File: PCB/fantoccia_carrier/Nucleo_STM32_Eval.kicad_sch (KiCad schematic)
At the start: 11 parts, among them J1 BU2450SM-JJ-GTR, U1 NUCLEO144-H743ZI

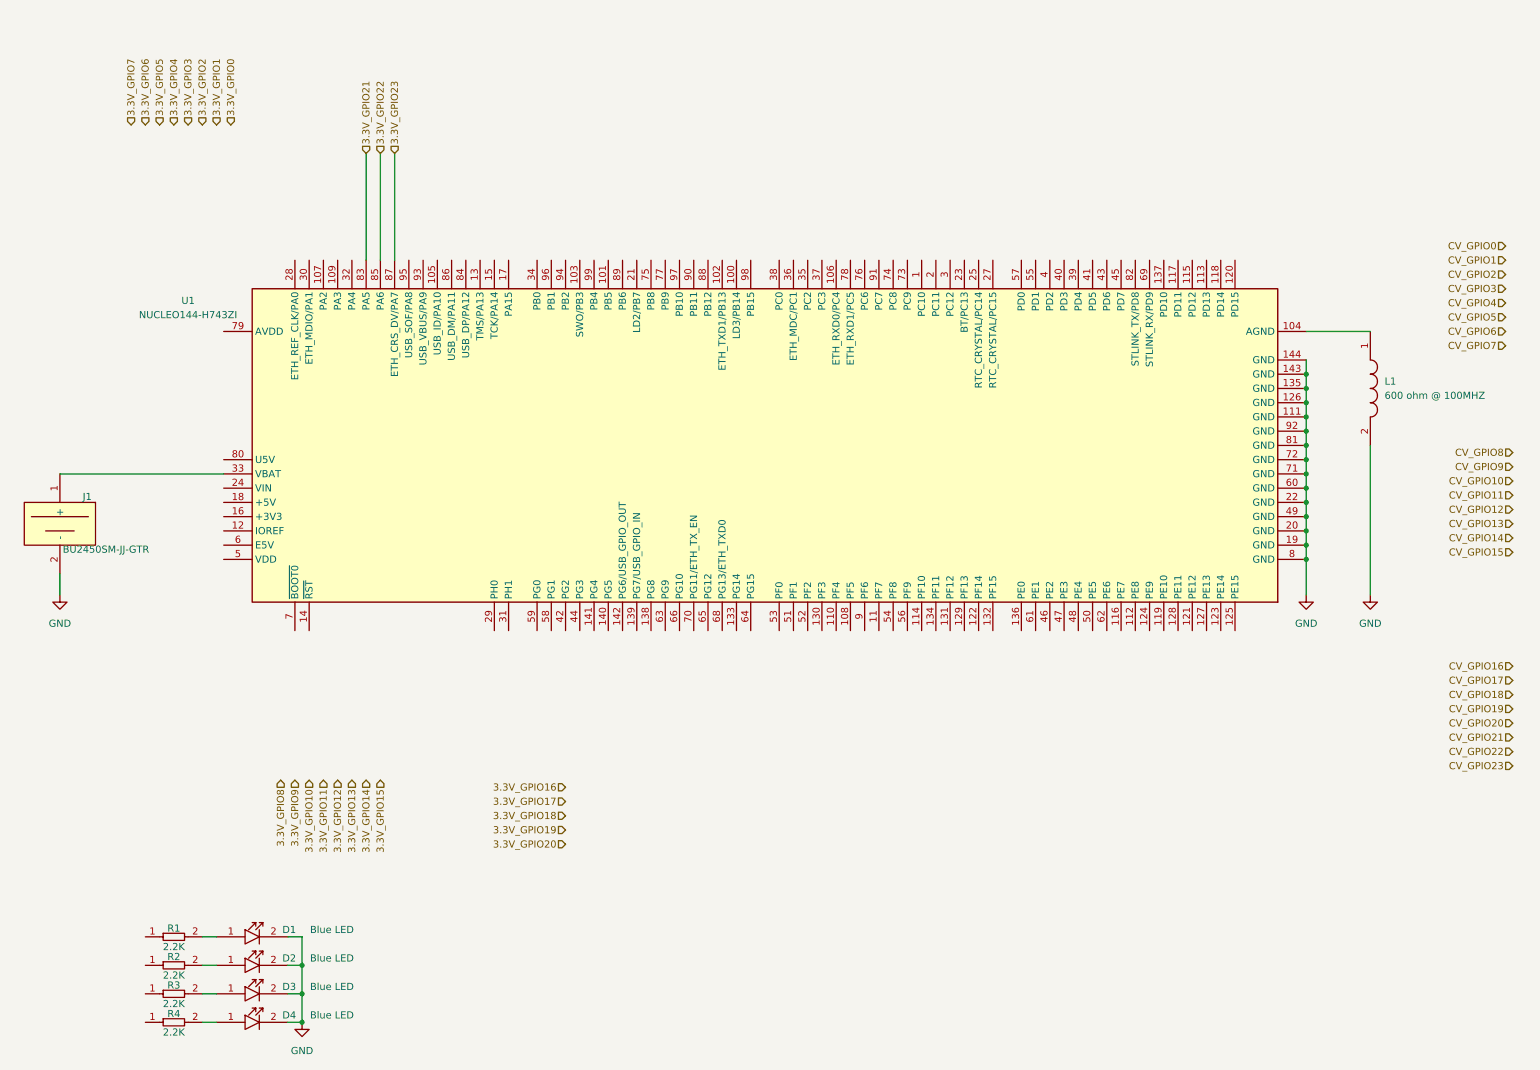
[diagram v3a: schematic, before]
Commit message: PCB and Pinout
Progress made with PCB wiring eval board pins to pheonix connectors. Pinout almost completely chosen but subject to revision !
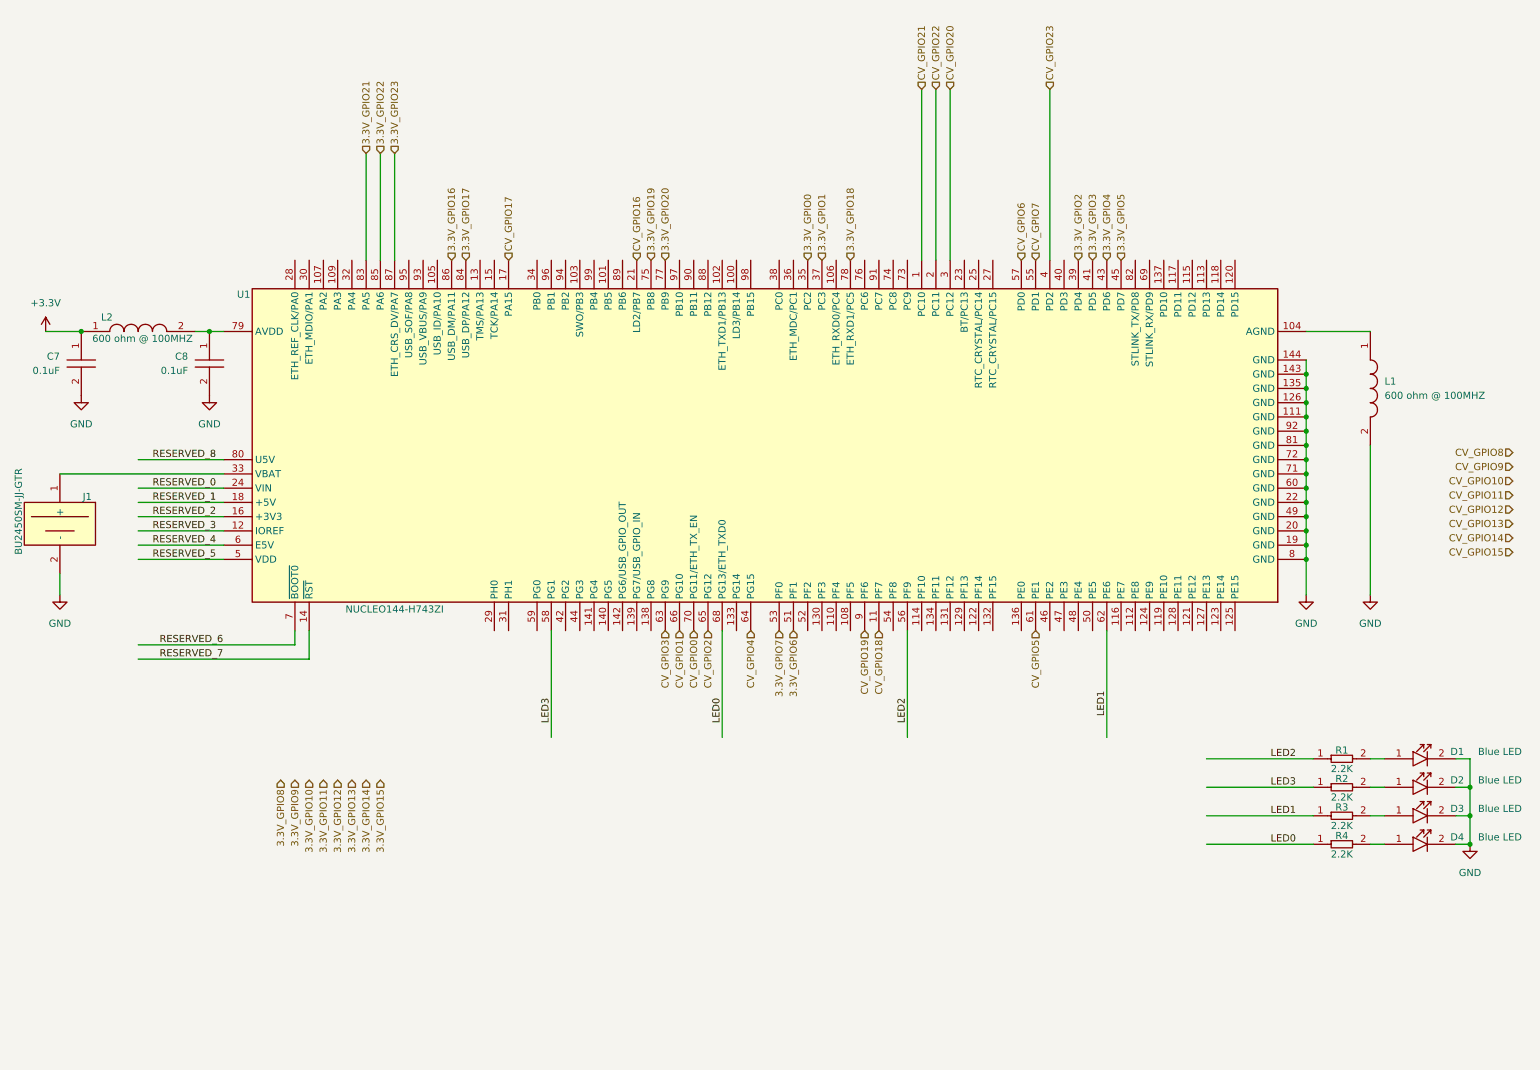
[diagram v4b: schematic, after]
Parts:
- added C7, C8: CGA3E2X7R1H104K080AA, AVR-KiCAD-Lib-Capacitors:C0603, symbol AVR-KiCAD-Lib-Capacitors:CGA3E2X7R1H104K080AA
- added L2: HZ0805E601R-10, AVR-KiCAD-Lib-Inductors:HZ0805E601R-10, symbol AVR-KiCAD-Lib-Inductors:HZ0805E601R-10
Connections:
- net 3.3V_GPIO0: now also U1.35 (PC2)
- net 3.3V_GPIO1: now also U1.37 (PC3)
- net 3.3V_GPIO16: now also U1.86 (USB_DM/PA11)
- net 3.3V_GPIO17: now also U1.84 (USB_DP/PA12)
- net 3.3V_GPIO18: now also U1.78 (ETH_RXD1/PC5)
- net 3.3V_GPIO19: now also U1.75 (PB8)
- net 3.3V_GPIO2: now also U1.39 (PD4)
- net 3.3V_GPIO20: now also U1.77 (PB9)
- net 3.3V_GPIO3: now also U1.41 (PD5)
- net 3.3V_GPIO4: now also U1.43 (PD6)
- net 3.3V_GPIO5: now also U1.45 (PD7)
- net 3.3V_GPIO6: now also U1.51 (PF1)
- net 3.3V_GPIO7: now also U1.53 (PF0)
- net CV_GPIO0: now also U1.70 (PG11/ETH_TX_EN)
- net CV_GPIO1: now also U1.66 (PG10)
- net CV_GPIO16: now also U1.21 (LD2/PB7)
- net CV_GPIO17: now also U1.17 (PA15)
- net CV_GPIO18: now also U1.11 (PF7)
- net CV_GPIO19: now also U1.9 (PF6)
- net CV_GPIO2: now also U1.65 (PG12)
- net CV_GPIO20: now also U1.3 (PC12)
- net CV_GPIO21: now also U1.1 (PC10)
- net CV_GPIO22: now also U1.2 (PC11)
- net CV_GPIO23: now also U1.4 (PD2)
- net CV_GPIO3: now also U1.63 (PG9)
- net CV_GPIO4: now also U1.64 (PG15)
- net CV_GPIO5: now also U1.61 (PE1)
- net CV_GPIO6: now also U1.57 (PD0)
- net CV_GPIO7: now also U1.55 (PD1)
- net GND: now also C7.2, C8.2
- net LED0: now reaches R4.1
- net LED0: now also U1.68 (PG13/ETH_TXD0)
- net RESERVED_3: now reaches U1.12 (IOREF)
- net RESERVED_7: now reaches U1.14 (~{RST})
- net RESERVED_2: now reaches U1.16 (+3V3)
- net RESERVED_1: now reaches U1.18 (+5V)
- net RESERVED_0: now reaches U1.24 (VIN)
- net RESERVED_5: now reaches U1.5 (VDD)
- net LED2: now reaches U1.56 (PF9)
- net LED2: now also R1.1
- net LED3: now reaches U1.58 (PG1)
- net LED3: now also R2.1
- net RESERVED_4: now reaches U1.6 (E5V)
- net LED1: now reaches U1.62 (PE6)
- net LED1: now also R3.1
- net RESERVED_6: now reaches U1.7 (~{BOOT0})
- net at U1.79 (AVDD): now also C8.1, L2.2
- net RESERVED_8: now reaches U1.80 (U5V)
- new net +3.3V: C7.1, L2.1
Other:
- moved on the sheet: D1, D2, D3, D4, R1, R2, R3, R4
